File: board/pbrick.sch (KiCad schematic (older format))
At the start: 58 parts, among them J1 UJC-HP-3-SMT-TR, J2 TC2030-IDC-NL, J3 U.FL2PIN, J4 QWIIC, J5 5055670271, M0 5055680471, M1 5055680471, Q1 SSM6J507NU, Q2 SSM6J507NU, U1 MIC5219-3.3YML-TR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

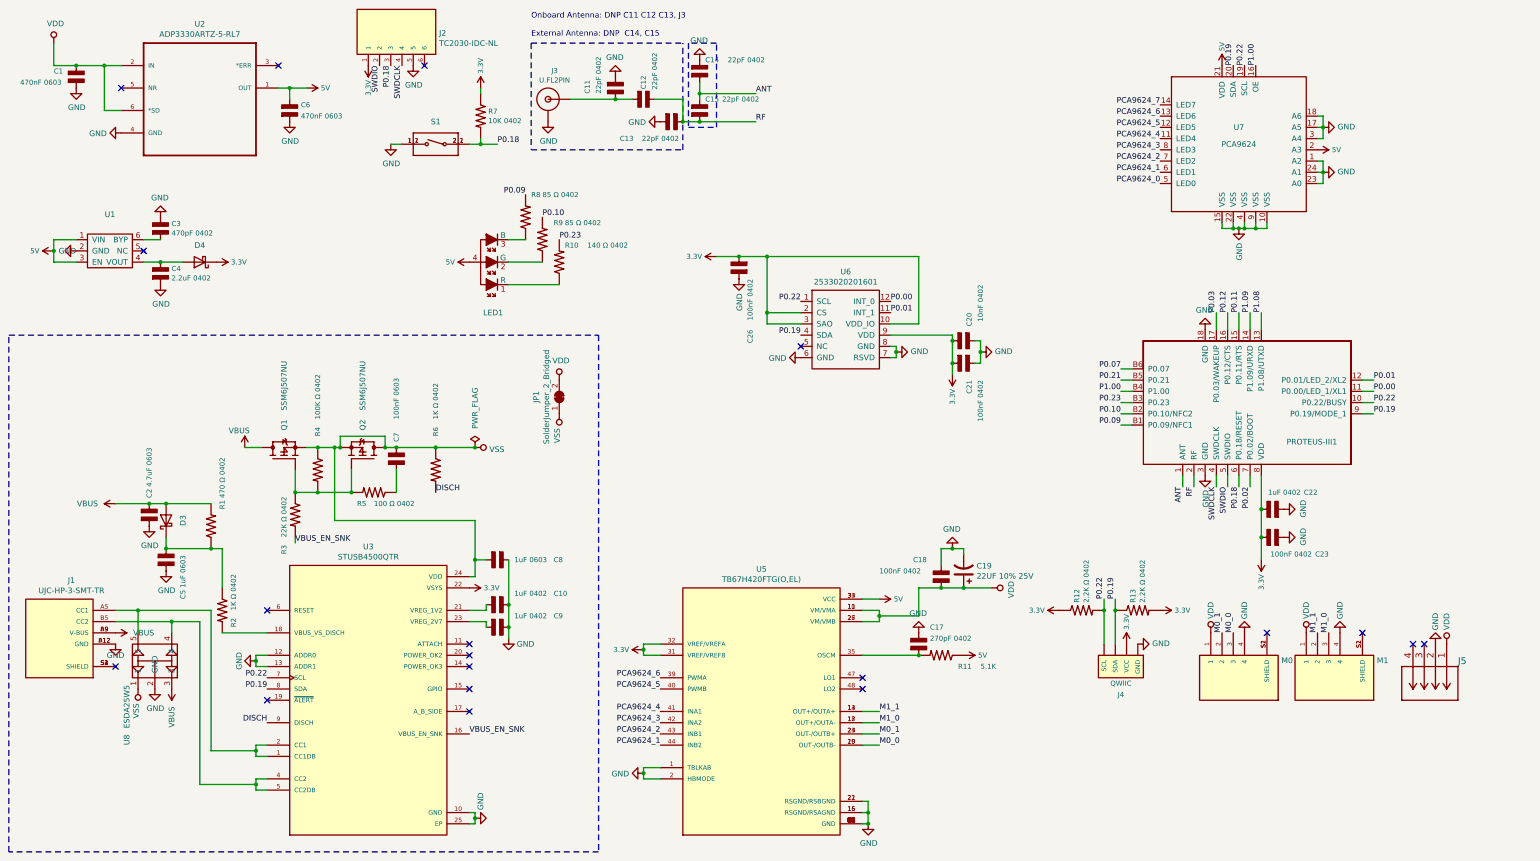
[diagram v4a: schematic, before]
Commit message: Reverting to APP_PWM from board
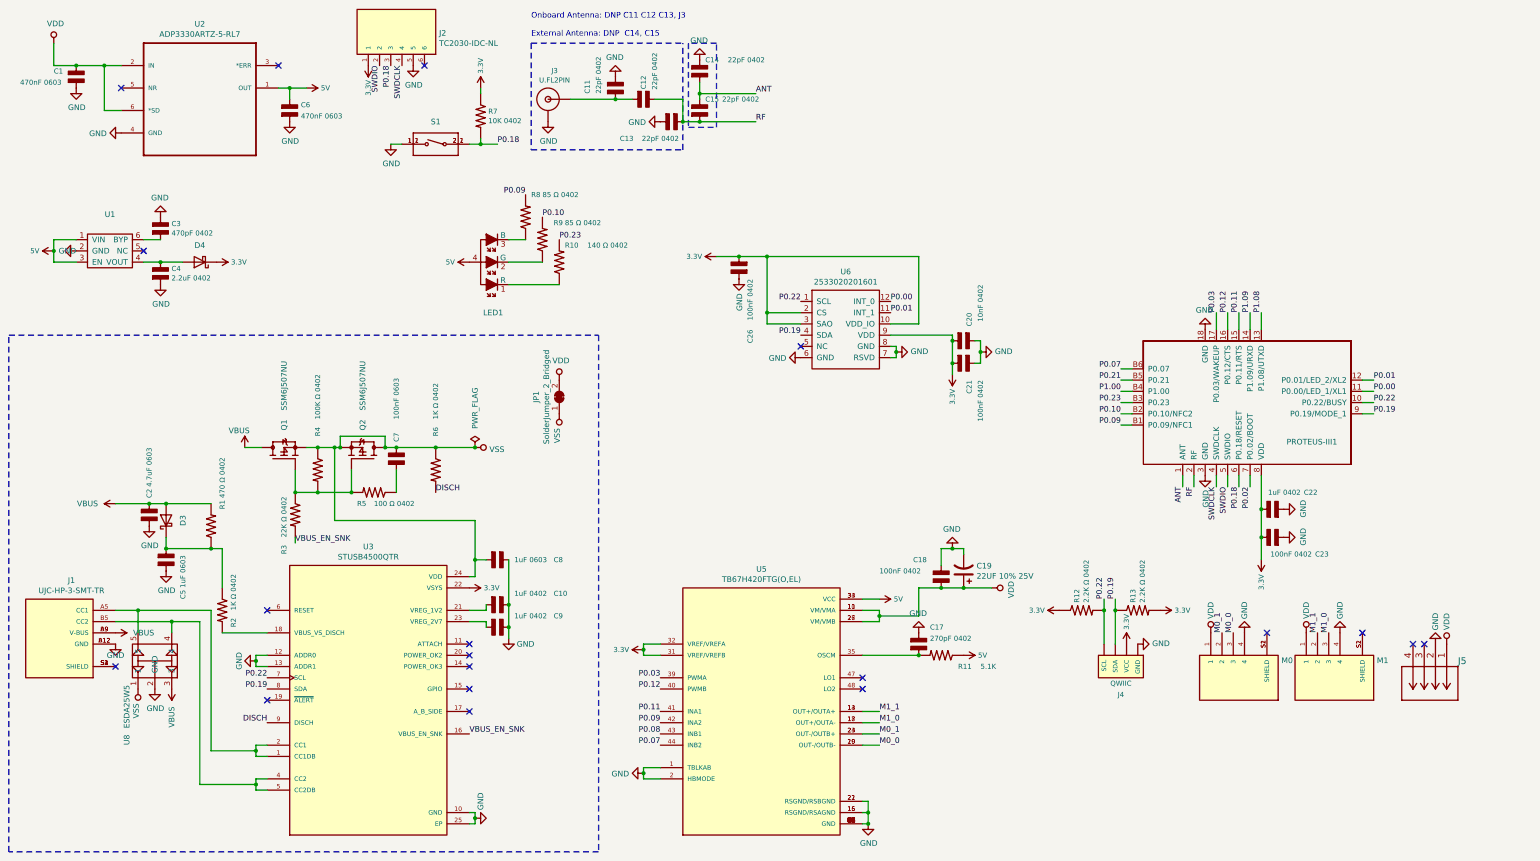
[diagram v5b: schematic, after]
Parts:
- removed U7: PCA9624, Package_DFN_QFN:QFN-24-1EP_4x4mm_P0.5mm_EP2.65x2.65mm_ThermalVias, symbol pbrick:PCA9624
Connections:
- net PCA9624_1 is gone; now on net P0.07: U5.44 (INB2)
- net PCA9624_3 is gone; now on net P0.09: U5.42 (INA2)
- net PCA9624_4 is gone; now on net P0.11: U5.41 (INA1)
- net PCA9624_5 is gone; now on net P0.12: U5.40 (PWMB)
- net PCA9624_6 is gone; now on net P0.03: U5.39 (PWMA)
- net PCA9624_2 renamed P0.08
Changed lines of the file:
@@
 Text Label 11600 3250 1    50   ~ 0
 P1.08
-Text Label 11350 1050 1    50   ~ 0
-P0.19
-Text Label 11450 1050 1    50   ~ 0
-P0.22
-$Comp
-L power:GND #PWR051
-U 1 1 6056D0AD
-P 11400 2500
-F 0 "#PWR051" H 11400 2250 50  0001 C CNN
-F 1 "GND" V 11405 2372 50  0000 R CNN
-F 2 "" H 11400 2500 50  0001 C CNN
-F 3 "" H 11400 2500 50  0001 C CNN
-	1    11400 2500
-	1    0    0    -1
-$EndComp
-Text Label 10700 2100 2    50   ~ 0
-PCA9624_0
-Text Label 10700 2000 2    50   ~ 0
-PCA9624_1
-Text Label 10700 1900 2    50   ~ 0
-PCA9624_2
-Text Label 10700 1800 2    50   ~ 0
-PCA9624_3
-Text Label 10700 1700 2    50   ~ 0
-PCA9624_4
-Text Label 10700 1600 2    50   ~ 0
-PCA9624_5
-Text Label 10700 1500 2    50   ~ 0
-PCA9624_6
-Text Label 10700 1400 2    50   ~ 0
-PCA9624_7
 Text Label 8300 3250 0    50   ~ 0
 P0.01
@@
 P0.22
 $Comp
-L pbrick-rescue:5V-SparkFun-PowerSymbols #SUPPLY0101
-U 1 1 604DCCBD
-P 11250 1050
-F 0 "#SUPPLY0101" H 11300 1050 45  0001 L BNN
-F 1 "5V" V 11250 1178 45  0000 L CNN
-F 2 "XXX-00000" V 11292 1178 60  0001 L CNN
-F 3 "" H 11250 1050 60  0001 C CNN
-	1    11250 1050
-	1    0    0    -1
-$EndComp
-$Comp
 L pbrick-rescue:3.3V-SparkFun-PowerSymbols #SUPPLY0103
 U 1 1 605C136D
@@
 Text Label 12200 6100 1    50   ~ 0
 M1_0
-$Comp
-L pbrick:PCA9624 U7
-U 1 1 6035C8D6
-P 11400 1800
-F 0 "U7" H 11400 2000 50  0000 C CNN
-F 1 "PCA9624" H 11400 1850 50  0000 C CNN
-F 2 "Package_DFN_QFN:QFN-24-1EP_4x4mm_P0.5mm_EP2.65x2.65mm_ThermalVias" H 11450 1800 50  0001 C CNN
-F 3 "https://www.nxp.com/docs/en/data-sheet/PCA9624.pdf" H 11450 1800 50  0001 C CNN
-F 4 "NXP USA Inc." H 11400 1800 50  0001 C CNN "Manufacturer"
-F 5 "PCA9624BS,118" H 11400 1800 50  0001 C CNN "MPN"
-F 6 "568-5304-1-ND" H 11400 1800 50  0001 C CNN "Digi-Key_PN"
-F 7 "IC LED DRIVER LINEAR DIM 24HVQFN" H 11400 1800 50  0001 C CNN "Description"
-	1    11400 1800
-	1    0    0    -1
-$EndComp
-Wire Wire Line
-	11650 2500 11650 2450
-Wire Wire Line
-	11550 2450 11550 2500
-Connection ~ 11550 2500
-Wire Wire Line
-	11550 2500 11650 2500
-Wire Wire Line
-	11450 2450 11450 2500
-Connection ~ 11450 2500
-Wire Wire Line
-	11450 2500 11550 2500
-Wire Wire Line
-	11350 2450 11350 2500
-Connection ~ 11350 2500
-Wire Wire Line
-	11350 2500 11400 2500
-Wire Wire Line
-	11250 2450 11250 2500
-Wire Wire Line
-	11250 2500 11350 2500
-Connection ~ 11400 2500
-Wire Wire Line
-	11400 2500 11450 2500
-Wire Wire Line
-	12100 1900 12150 1900
-Wire Wire Line
-	12150 1900 12150 2000
-Wire Wire Line
-	12150 2100 12100 2100
-Wire Wire Line
-	12100 2000 12150 2000
-Connection ~ 12150 2000
-Wire Wire Line
-	12150 2000 12150 2100
-Wire Wire Line
-	12100 1700 12150 1700
-Wire Wire Line
-	12150 1700 12150 1600
-Wire Wire Line
-	12150 1500 12100 1500
-Wire Wire Line
-	12100 1600 12150 1600
-Connection ~ 12150 1600
-Wire Wire Line
-	12150 1600 12150 1500
-$Comp
-L pbrick-rescue:5V-SparkFun-PowerSymbols #SUPPLY0106
-U 1 1 60422EE3
-P 12100 1800
-F 0 "#SUPPLY0106" H 12150 1800 45  0001 L BNN
-F 1 "5V" V 12100 1928 45  0000 L CNN
-F 2 "XXX-00000" V 12142 1928 60  0001 L CNN
-F 3 "" H 12100 1800 60  0001 C CNN
-	1    12100 1800
-	0    1    1    0
-$EndComp
-$Comp
-L power:GND #PWR0107
-U 1 1 6042343E
-P 12150 2000
-F 0 "#PWR0107" H 12150 1750 50  0001 C CNN
-F 1 "GND" V 12155 1872 50  0000 R CNN
-F 2 "" H 12150 2000 50  0001 C CNN
-F 3 "" H 12150 2000 50  0001 C CNN
-	1    12150 2000
-	0    -1   -1   0
-$EndComp
-$Comp
-L power:GND #PWR0108
-U 1 1 60423B66
-P 12150 1600
-F 0 "#PWR0108" H 12150 1350 50  0001 C CNN
-F 1 "GND" V 12155 1472 50  0000 R CNN
-F 2 "" H 12150 1600 50  0001 C CNN
-F 3 "" H 12150 1600 50  0001 C CNN
-	1    12150 1600
-	0    -1   -1   0
-$EndComp
 Text Label 6250 7100 2    50   ~ 0
-PCA9624_1
+P0.07
 Text Label 6250 7000 2    50   ~ 0
-PCA9624_2
+P0.08
 Text Label 6250 6900 2    50   ~ 0
-PCA9624_3
+P0.09
 Text Label 6250 6800 2    50   ~ 0
-PCA9624_4
+P0.11
 Text Label 6250 6600 2    50   ~ 0
-PCA9624_5
+P0.12
 Text Label 6250 6500 2    50   ~ 0
-PCA9624_6
+P0.03
 $Comp
 L power:GND #PWR0109
@@
 	0    1    1    0
 $EndComp
-Text Label 11550 1050 1    50   ~ 0
-P1.00
 Wire Wire Line
 	2650 6300 2650 6350

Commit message: Wrong board wiring again...
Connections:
- net P0.08 is gone; now on net P1.08: U5.43 (INB1)
- net P0.09: no longer U5.42 (INA2)
- net P1.09: now also U5.42 (INA2)
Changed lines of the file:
@@
 P0.07
 Text Label 6250 7000 2    50   ~ 0
-P0.08
+P1.08
 Text Label 6250 6900 2    50   ~ 0
-P0.09
+P1.09
 Text Label 6250 6800 2    50   ~ 0
 P0.11

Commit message: Minor board update
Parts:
- JP1: footprint Jumper:SolderJumper-2_P1.3mm_Bridged_Pad1.0x1.5mm -> Jumper:SolderJumper-2_P1.3mm_Open_Pad1.0x1.5mm
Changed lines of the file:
@@
 F 0 "JP1" H 5350 4205 50  0000 C CNN
 F 1 "SolderJumper_2_Bridged" H 5350 4114 50  0000 C CNN
-F 2 "Jumper:SolderJumper-2_P1.3mm_Bridged_Pad1.0x1.5mm" H 5350 4000 50  0001 C CNN
+F 2 "Jumper:SolderJumper-2_P1.3mm_Open_Pad1.0x1.5mm" H 5350 4000 50  0001 C CNN
 F 3 "~" H 5350 4000 50  0001 C CNN
 	1    5350 4000

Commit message: Updating Board layout, pcb, board definition
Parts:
- C20: value 10nF 0402 -> 100nF 0402; Digi-Key_PN 732-7989-1-ND -> 732-7495-1-ND; MPN 885012206071 -> 885012105018
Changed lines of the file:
@@
 P 8950 3500
 F 0 "C20" H 8700 3550 45  0000 L CNN
-F 1 "10nF 0402" H 8450 3650 45  0000 L CNN
+F 1 "100nF 0402" H 8450 3650 45  0000 L CNN
 F 2 "Capacitor_SMD:C_0402_1005Metric" H 9200 3410 20  0001 C CNN
 F 3 "https://www.we-online.de/katalog/datasheet/885012006019.pdf" H 8950 3500 60  0001 C CNN
-F 4 "732-7989-1-ND" H 8950 3500 50  0001 C CNN "Digi-Key_PN"
+F 4 "732-7495-1-ND" H 8950 3500 50  0001 C CNN "Digi-Key_PN"
 F 5 "Würth Elektronik" H 8950 3500 50  0001 C CNN "Manufacturer"
-F 6 "885012206071" H 8950 3500 50  0001 C CNN "MPN"
+F 6 "885012105018" H 8950 3500 50  0001 C CNN "MPN"
 F 7 "CAP CER 0.1UF 25V X5R 0402" H 8950 3500 50  0001 C CNN "Description"
 	1    8950 3500
